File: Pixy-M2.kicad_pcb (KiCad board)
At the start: 4 copper layers, 66 x 100 mm, 78 parts, among them J1 USB_C_Receptacle_USB2.0_14P, J10 SM09B-SRSS-TB, J11 SM06B-SRSS-TB, J4 SM06B-SRSS-TB, J5 SM06B-SRSS-TB, J6 SM06B-SRSS-TB, J7 SM06B-SRSS-TB, J8 S6B-PH-K, J9 S6B-PH-K, Q1 AO4407A, SW1 SW_Push, SW2 SW_Push, SW3 JS102011SAQN, U1 ESP32-S3-WROOM-1-N16, U2 USBLC6-2SC6, U3 AP63203WU, U4 DRV8231ADSG, U5 DRV8231ADSG

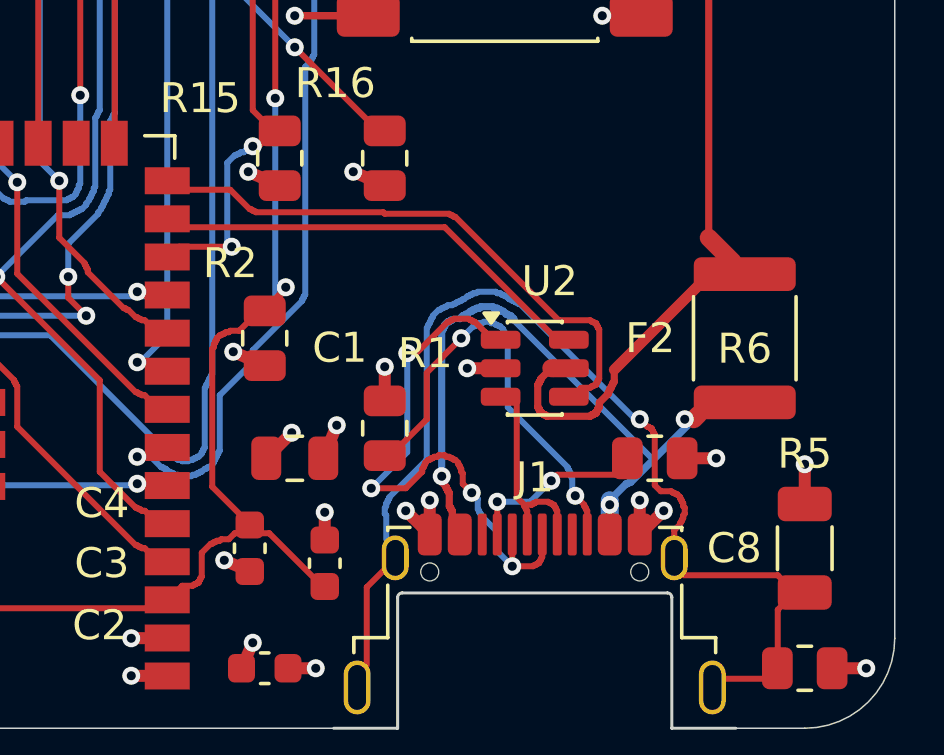
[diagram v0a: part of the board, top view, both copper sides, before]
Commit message: layout: route USB as a coupled pair for review finding 7
D+/D- were ordinary 0.2 mm traces with varying separation, a D+ detour round
U2 and asymmetric layer changes; the issue-6 via pass had left the connector
side D- with 4 vias and 8 mm on B.Cu. Both polarities now run as one pair,
J1 -> U2 -> U1, entirely on F.Cu over the In1 plane, with no vias.

                                    before          after
  USB vias / B.Cu copper            4 / 8.01 mm     0 / 0
  width, module-side gap            0.20, 0.25-0.35 0.25, 0.15 mm
  J1->U2->U1 path, D+ / D-          24.54 / 32.62   20.15 / 19.11 mm
  end-to-end skew                   8.08 mm         1.04 mm (~6 ps)
  U2 GND pin to plane via           1.11 mm         0.71 mm

U2 turned 90 deg, (154,148) rot 0 -> (153.5,149.5) rot 90. USBLC6-2SC6 is
flow-through (1->6, 3->4); at rot 0 that ran across the signal direction, so
D+ had to wrap the part. Now the connector row faces J1 and the module row
faces U1, D- west in both. U2's middle pins leave under the body between the
pin rows: GND to a plane via under the package, VBUS east to the F2 feed.
J1's alternating D-/D+/D-/D+ pads are joined on F.Cu (D+ bridge over A7, D-
loop under A6). CC1/CC2 re-searched around the pair, crossing on B.Cu.

0.25/0.15 mm is field-solved for this stackup (tools/impedance/zdiff.py):
~88-94 ohm across 0.200/0.2104 mm prepreg and 10-25 um mask. The earlier
CLAUDE.md guess of 0.2/0.15 mm solves to ~100 ohm. Confirm with the fab.

Rules: a USB netclass (0.25 mm, 0.15 mm gap, 0.15 mm clearance inside the
class) and DRC rules for width, F.Cu only, and pair gap / uncoupled length.
Each fired on a deliberately broken copy of the board.

The stage is tools/autoroute/usb_pair.py, run last in rework.py so every
earlier stage replays unchanged; pcbedit gains sync() so a late footprint move
no longer drops pending track edits. The rework.py replay was first checked
to reproduce 0c70856 exactly.

DRC unchanged: 0 unconnected, 0 parity, only the four J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
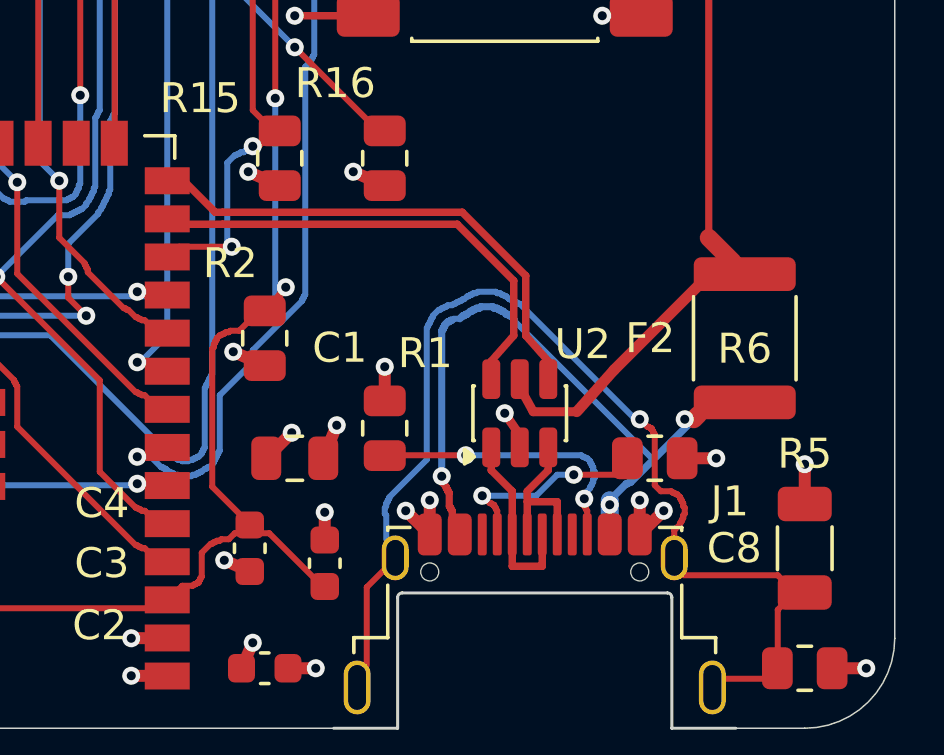
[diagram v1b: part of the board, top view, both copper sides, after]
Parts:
- moved U2 1.58 mm to (153.5, 149.5), turned to 90 degrees
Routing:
- net Net-(J1-D--PadA7): track 17.9 -> 4.35 mm, vias 4 -> 0
- net Net-(J1-CC2): track 13.6 -> 8.53 mm
- net /USB_D+: track 18.4 -> 16.0 mm
- net Net-(J1-D+-PadA6): track 5.52 -> 3.90 mm
- net /VBUS: track 92.6 -> 91.2 mm
- net /USB_D-: track 13.7 -> 15.0 mm
- net Net-(J1-CC1): track 4.92 -> 5.81 mm

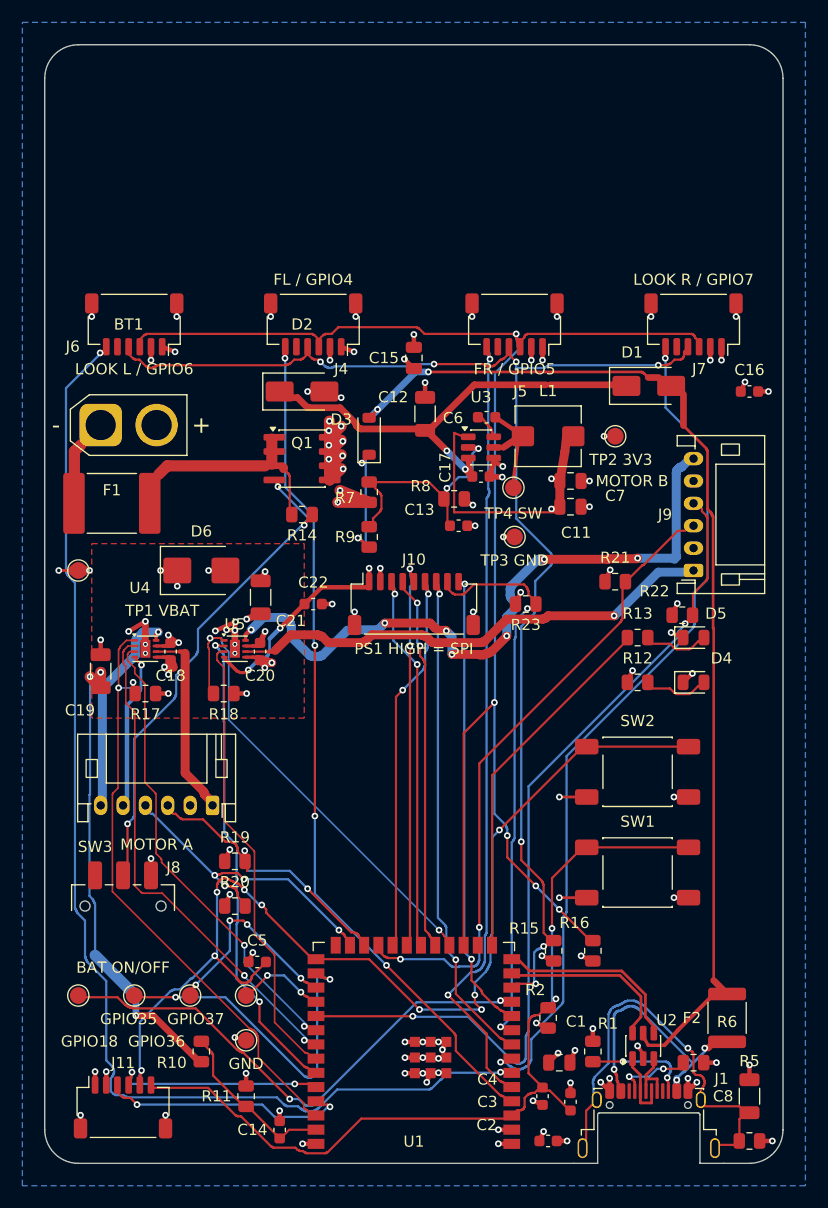
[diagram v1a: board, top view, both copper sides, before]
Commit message: layout: encode the routing requirements as rules for review finding 8
The project rules let narrow copper pass anywhere: one Default netclass and a
0.15 mm global minimum. Findings 1 and 7 added the Motor and USB rules; this
adds the rest, and fixes the copper the new rules caught.

Rules:
  Battery netclass (/VBAT_RAW, /VBAT_FUSED) 1.0 mm, DRC floor 0.8 mm
  Power netclass (/VBUS, /VSYS, Net-(F2-Pad1)) 0.6 mm, floor 0.5 mm, except
    U2's VBUS pin under the package ('Power pin escape' area)
  every track >= 0.2 mm except in the DRV8231A pin fields
  clearance floors: REG_EN to SW/BST 0.35 mm; REG_EN and VBAT_SENSE to motor
    copper (and VBAT_SENSE to SW) 5 mm; IPROPI to motor copper 0.25 mm
/VBAT is in neither supply class: its current runs in the In2 island.

KiCad behaviours the rules depend on, all verified: the board-setup minimum is
absolute (custom rules cannot relax it), so it stays 0.15 mm and the 0.2 mm
floor is a custom rule; the later of two rules on one constraint wins, so the
generic rule must stay first in the file; enclosedByArea tests the whole track
outline including round caps.

Copper the rules required (tools/autoroute/issue8.py, after usb_pair.py):
                                    before          after
  track below 0.2 mm                219.4 mm        8.7 mm, pin fields only
  /VBUS F2 -> D1                    0.24 mm 105 mOhm 0.6 mm 44 mOhm
  J1.A9 / J1.A4 -> F2               9.7 / 32.7 mOhm 4.0 / 8.2 mOhm
  /VBAT_FUSED R14 tap               0.2 mm          0.8 mm
The five 0.15 mm nets (GPIO39-41 motor IN, GPIO2/10 IPROPI) were narrow end to
end; the USB supply was 0.24 mm despite the 0.6 mm width table. The D3 tap is
pinned to its old corridor: unpinned, A* ran it 0.5 mm from C6's switch-node
pad, and it feeds REG_EN through R9.

Two clearance floors are set under what CLAUDE.md asks and recorded as such:
REG_EN is 0.40 mm from the SW pin (the EN via under U3; CLAUDE.md's 0.99 mm
was not the closest pair and is corrected), IPROPI 0.29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
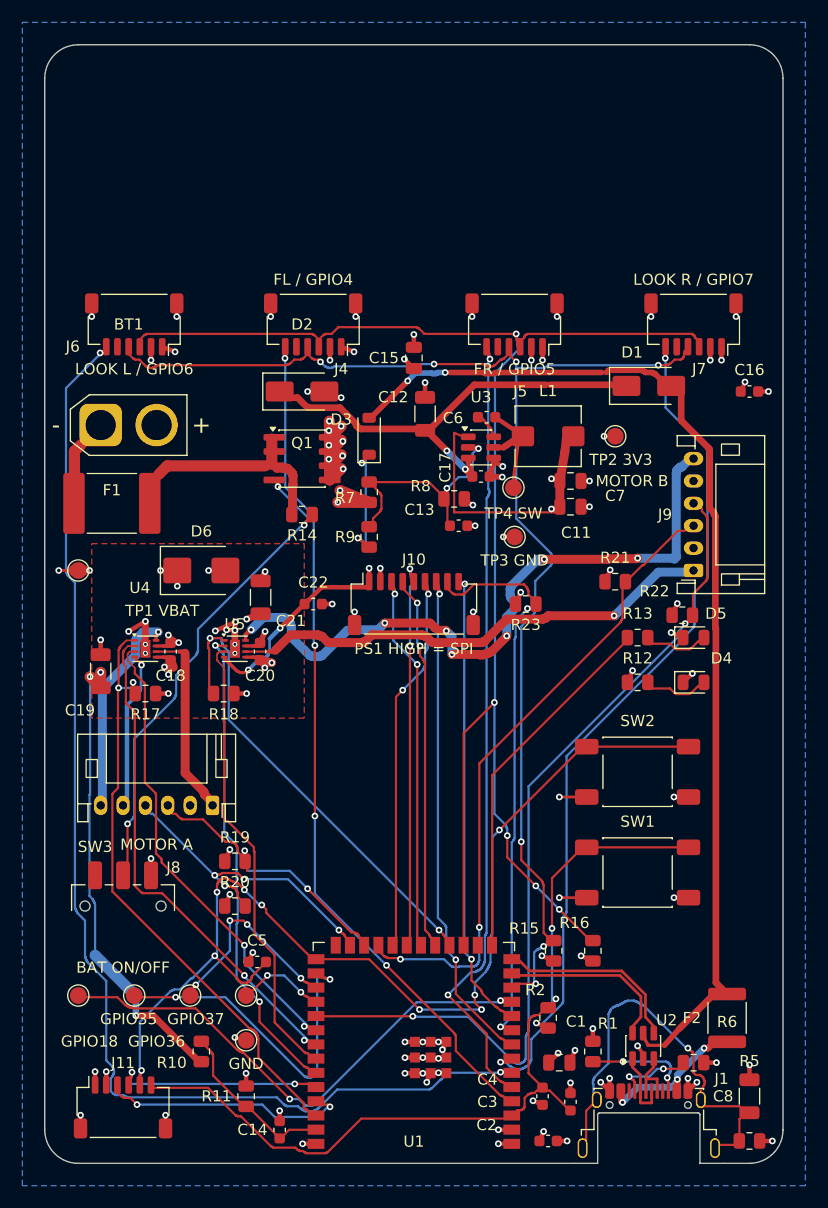
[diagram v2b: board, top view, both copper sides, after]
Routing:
- net Net-(F2-Pad1): track 22.1 -> 11.6 mm
- net /VBAT_FUSED: track 15.6 -> 17.2 mm
- net /VBUS: track 91.2 -> 90.4 mm

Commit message: layout: clear the J1 hole-clearance errors and the U1 footprint warning
The five DRC items carried since placement are resolved without changing any
copper, footprint geometry or placement. DRC: 0 violations, 0 unconnected,
0 schematic parity issues. ERC stays 0.

J1: the stock Amphenol 12401948E412A footprint puts its GND pads 0.25 mm from
its own 0.6 mm locating holes - the land pattern KiCad's librarians merged
against Amphenol drawing c12401948 (kicad-footprints MR !3540). JLCPCB states
0.20 mm NPTH-to-track. The land pattern stays. Board-setup hole clearance is
absolute (custom rules cannot relax it), so it goes 0.30 -> 0.20 mm and a new
"Hole clearance" rule restores 0.30 mm for every pair except J1's own pads
against J1's own holes. Tested both ways: a track 0.25 mm from an SW3 hole
still fails at 0.30 mm; J1's hole moved to 0.15 mm fails the 0.20 mm floor.
CLAUDE.md wrongly named the unused USB_C_Receptacle_Amazon footprint; fixed.

U1: the board copy differed from PCM_Espressif:ESP32-S3-WROOM-1 in five items,
the antenna outline and label moved from F.SilkS to F.Fab because the antenna
overhangs the board edge. That intentional variant is now a real footprint,
Pixy-M2.pretty/ESP32-S3-WROOM-1_AntennaOverhang (Espressif's file with only
those five layer changes), registered in a project fp-lib-table. U1 points at
it in the board and in the schematic's placed instance; the cached library
symbol is left as Espressif's, since editing it raises lib_symbol_mismatch.
rework.py sets the same id via the new Pcb.set_fpid; a replay reproduces the
committed tracks and vias exactly. The board file was edited in one line
rather than regenerated, to avoid UUID churn.

Evidence: layout/drc-clean/.

Co-Authored-By: Claude Opus 5.5 <noreply@anthropic.com>
Claude-Session: https://claude.ai/code/session_01MLrob72MX5PcwtzVMbc3bs
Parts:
- U1: footprint PCM_Espressif:ESP32-S3-WROOM-1 -> Pixy-M2:ESP32-S3-WROOM-1_AntennaOverhang
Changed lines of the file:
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@@
 		)
 	)
-	(footprint "PCM_Espressif:ESP32-S3-WROOM-1"
+	(footprint "Pixy-M2:ESP32-S3-WROOM-1_AntennaOverhang"
 		(layer "F.Cu")
 		(at 133 150 180)
